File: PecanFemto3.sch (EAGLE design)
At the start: 35 parts, among them U1 TPS62203DBVT

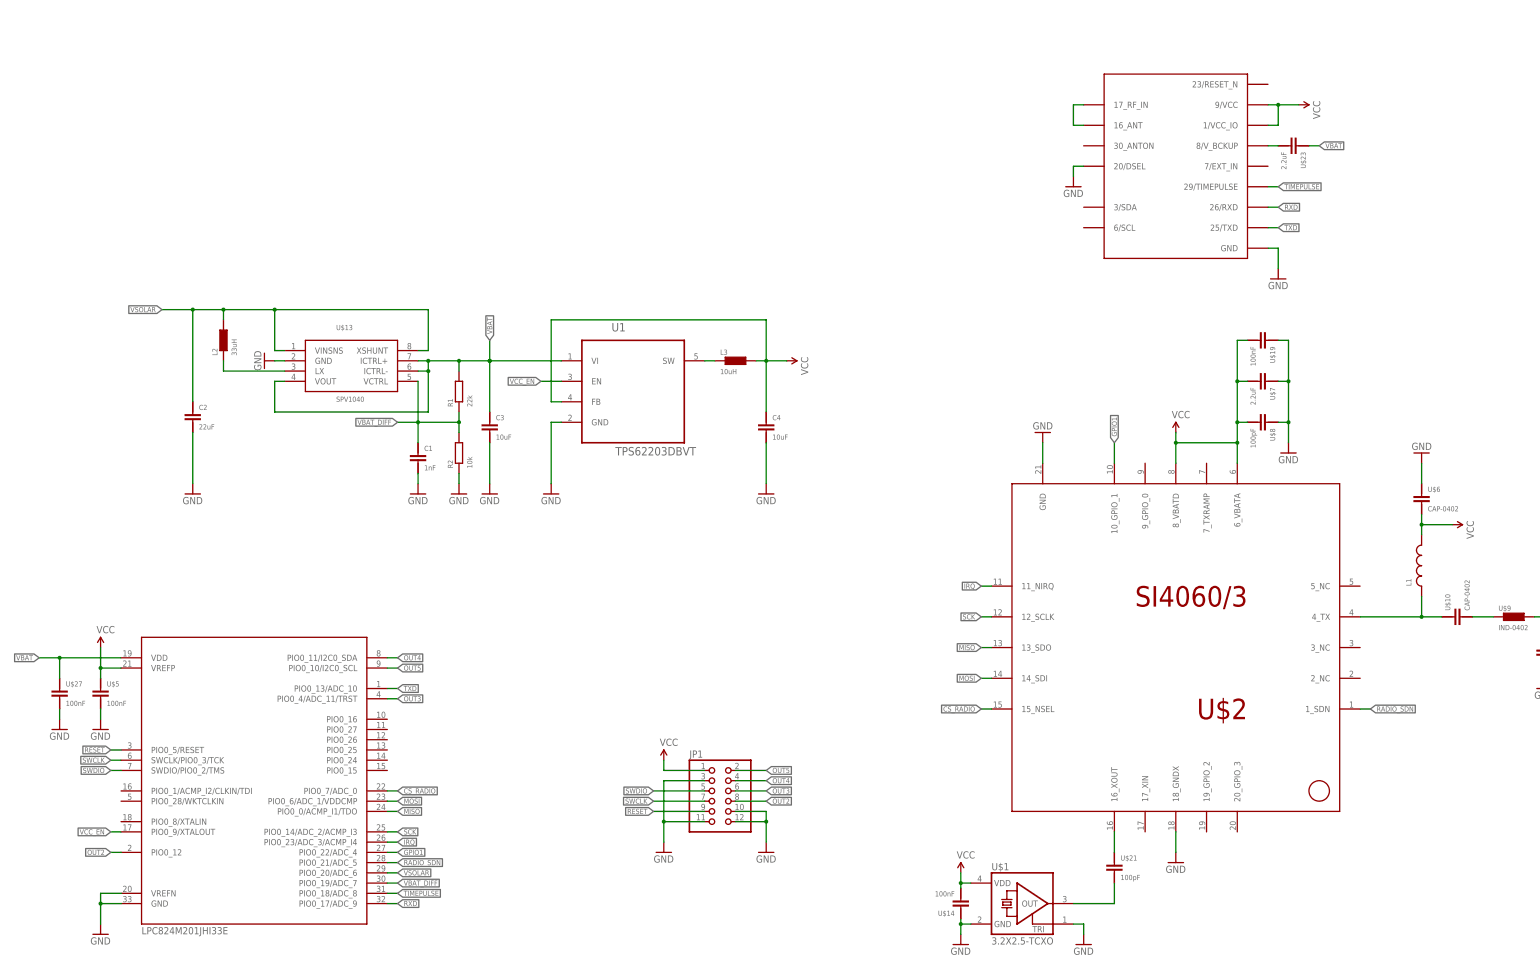
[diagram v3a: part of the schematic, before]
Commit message: Moved parts around, added MOSFET switch for GPS
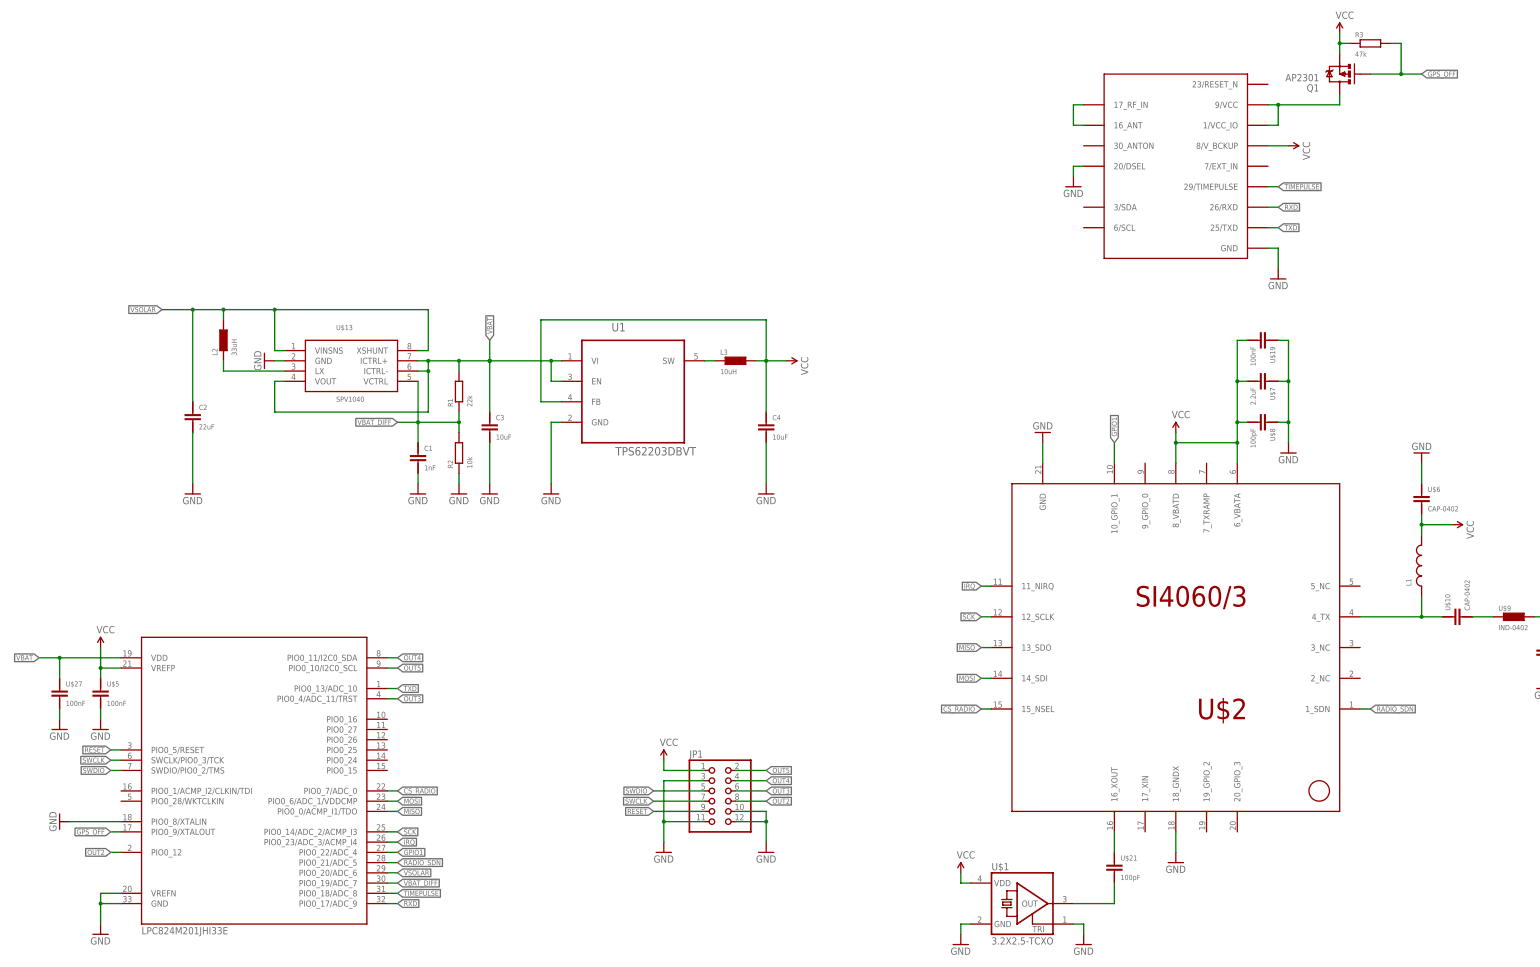
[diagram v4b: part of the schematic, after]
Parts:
- removed U$14: 100nF, sven:CAP-0402
- removed U$23: 2.2uF, sven:CAP-0603
- added Q1: AP2301, PecanPico6:MOSFET-PCHANNEL
- added R3: 47k, PecanPico6:RES-0402
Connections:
- removed net N$1: U$23.1, U$3.8/V_BCKUP
- removed net VCC_EN: U$4.PIO0_9/XTALOUT, U1.EN
- new net GPS_OFF: Q1.G, R3.2, U$4.PIO0_9/XTALOUT
- new net N$16: Q1.D, U$3.1/VCC_IO, U$3.9/VCC
- net GND: now also U$4.PIO0_8/XTALIN; no longer U$14.2
- net VBAT: now also U1.EN; no longer U$23.2
- net VCC: now also Q1.S, R3.1, U$3.8/V_BCKUP; no longer U$14.1, U$3.1/VCC_IO, U$3.9/VCC
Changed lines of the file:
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@@
 <part name="GND12" library="SparkFun-Aesthetics" deviceset="GND" device=""/>
 <part name="GND13" library="SparkFun-Aesthetics" deviceset="GND" device=""/>
-<part name="SUPPLY3" library="SparkFun-Aesthetics" deviceset="VCC" device=""/>
 <part name="SUPPLY4" library="SparkFun-Aesthetics" deviceset="VCC" device=""/>
 <part name="GND7" library="SparkFun-Aesthetics" deviceset="GND" device=""/>
@@
 <part name="U$27" library="sven" deviceset="CAP-0402" device="" value="100nF"/>
 <part name="GND24" library="SparkFun-Aesthetics" deviceset="GND" device=""/>
-<part name="U$23" library="sven" deviceset="CAP-0603" device="" value="2.2uF"/>
 <part name="U$7" library="sven" deviceset="CAP-0402" device="" value="2.2uF"/>
 <part name="SUPPLY7" library="SparkFun-Aesthetics" deviceset="VCC" device=""/>
-<part name="U$14" library="sven" deviceset="CAP-0402" device="" value="100nF"/>
+<part name="Q1" library="PecanPico6" deviceset="MOSFET-PCHANNEL" device="" value="AP2301"/>
+<part name="R3" library="PecanPico6" deviceset="RES-0402" device="" value="47k"/>
+<part name="SUPPLY3" library="SparkFun-Aesthetics" deviceset="VCC" device=""/>
+<part name="SUPPLY8" library="SparkFun-Aesthetics" deviceset="VCC" device=""/>
+<part name="GND25" library="SparkFun-Aesthetics" deviceset="GND" device=""/>
 </parts>
 <sheets>
@@
 <instance part="GND12" gate="1" x="193.04" y="154.94"/>
 <instance part="GND13" gate="1" x="243.84" y="132.08"/>
-<instance part="SUPPLY3" gate="G$1" x="248.92" y="175.26" rot="R270"/>
 <instance part="SUPPLY4" gate="G$1" x="218.44" y="93.98"/>
 <instance part="GND7" gate="1" x="246.38" y="88.9"/>
@@
 <instance part="U$27" gate="G$1" x="-58.42" y="30.48"/>
 <instance part="GND24" gate="1" x="-58.42" y="20.32"/>
-<instance part="U$23" gate="G$1" x="248.92" y="165.1" rot="R270"/>
 <instance part="U$7" gate="G$1" x="241.3" y="106.68" rot="R270"/>
 <instance part="SUPPLY7" gate="G$1" x="91.44" y="12.7"/>
-<instance part="U$14" gate="G$1" x="165.1" y="-24.13" rot="R180"/>
+<instance part="Q1" gate="G$1" x="259.08" y="182.88" rot="R180"/>
+<instance part="R3" gate="G$1" x="266.7" y="190.5"/>
+<instance part="SUPPLY3" gate="G$1" x="259.08" y="193.04"/>
+<instance part="SUPPLY8" gate="G$1" x="246.38" y="165.1" rot="R270"/>
+<instance part="GND25" gate="1" x="-58.42" y="-2.54" rot="R270"/>
 </instances>
 <busses>
@@
 <pinref part="U$1" gate="G$1" pin="GND"/>
 <wire x1="165.1" y1="-27.94" x2="167.64" y2="-27.94" width="0.1524" layer="91"/>
-<pinref part="U$14" gate="G$1" pin="2"/>
-<wire x1="165.1" y1="-27.94" x2="165.1" y2="-26.67" width="0.1524" layer="91"/>
-<junction x="165.1" y="-27.94"/>
 </segment>
 <segment>
@@
 <pinref part="GND24" gate="1" pin="GND"/>
 </segment>
+<segment>
+<pinref part="U$4" gate="G$1" pin="PIO0_8/XTALIN"/>
+<wire x1="-43.18" y1="-2.54" x2="-55.88" y2="-2.54" width="0.1524" layer="91"/>
+<pinref part="GND25" gate="1" pin="GND"/>
+</segment>
 </net>
 <net name="N$4" class="0">
@@
 <junction x="279.4" y="71.12"/>
 <pinref part="SUPPLY1" gate="G$1" pin="VCC"/>
-</segment>
-<segment>
-<pinref part="U$3" gate="G$1" pin="1/VCC_IO"/>
-<wire x1="241.3" y1="170.18" x2="243.84" y2="170.18" width="0.1524" layer="91"/>
-<wire x1="243.84" y1="170.18" x2="243.84" y2="175.26" width="0.1524" layer="91"/>
-<pinref part="U$3" gate="G$1" pin="9/VCC"/>
-<wire x1="243.84" y1="175.26" x2="241.3" y2="175.26" width="0.1524" layer="91"/>
-<junction x="243.84" y="175.26"/>
-<wire x1="243.84" y1="175.26" x2="248.92" y2="175.26" width="0.1524" layer="91"/>
-<pinref part="SUPPLY3" gate="G$1" pin="VCC"/>
 </segment>
 <segment>
@@
 <wire x1="165.1" y1="-17.78" x2="165.1" y2="-15.24" width="0.1524" layer="91"/>
 <wire x1="167.64" y1="-17.78" x2="165.1" y2="-17.78" width="0.1524" layer="91"/>
-<pinref part="U$14" gate="G$1" pin="1"/>
-<wire x1="165.1" y1="-17.78" x2="165.1" y2="-19.05" width="0.1524" layer="91"/>
-<junction x="165.1" y="-17.78"/>
 </segment>
 <segment>
 <pinref part="U1" gate="A" pin="FB"/>
-<wire x1="66.04" y1="101.6" x2="63.5" y2="101.6" width="0.1524" layer="91"/>
-<wire x1="63.5" y1="101.6" x2="63.5" y2="121.92" width="0.1524" layer="91"/>
-<wire x1="63.5" y1="121.92" x2="116.84" y2="121.92" width="0.1524" layer="91"/>
+<wire x1="66.04" y1="101.6" x2="60.96" y2="101.6" width="0.1524" layer="91"/>
+<wire x1="60.96" y1="101.6" x2="60.96" y2="121.92" width="0.1524" layer="91"/>
+<wire x1="60.96" y1="121.92" x2="116.84" y2="121.92" width="0.1524" layer="91"/>
 <pinref part="L3" gate="G$1" pin="2"/>
 <wire x1="114.3" y1="111.76" x2="116.84" y2="111.76" width="0.1524" layer="91"/>
@@
 <wire x1="91.44" y1="10.16" x2="91.44" y2="12.7" width="0.1524" layer="91"/>
 <pinref part="SUPPLY7" gate="G$1" pin="VCC"/>
+</segment>
+<segment>
+<pinref part="Q1" gate="G$1" pin="S"/>
+<wire x1="259.08" y1="187.96" x2="259.08" y2="190.5" width="0.1524" layer="91"/>
+<pinref part="R3" gate="G$1" pin="1"/>
+<wire x1="259.08" y1="190.5" x2="259.08" y2="193.04" width="0.1524" layer="91"/>
+<wire x1="259.08" y1="190.5" x2="261.62" y2="190.5" width="0.1524" layer="91"/>
+<junction x="259.08" y="190.5"/>
+<pinref part="SUPPLY3" gate="G$1" pin="VCC"/>
+</segment>
+<segment>
+<pinref part="U$3" gate="G$1" pin="8/V_BCKUP"/>
+<pinref part="SUPPLY8" gate="G$1" pin="VCC"/>
+<wire x1="246.38" y1="165.1" x2="241.3" y2="165.1" width="0.1524" layer="91"/>
 </segment>
 </net>
@@
 <pinref part="C3" gate="G$1" pin="2"/>
 <pinref part="U1" gate="A" pin="VI"/>
-<wire x1="48.26" y1="111.76" x2="66.04" y2="111.76" width="0.1524" layer="91"/>
+<wire x1="48.26" y1="111.76" x2="63.5" y2="111.76" width="0.1524" layer="91"/>
 <junction x="48.26" y="111.76"/>
+<pinref part="U1" gate="A" pin="EN"/>
+<wire x1="63.5" y1="111.76" x2="66.04" y2="111.76" width="0.1524" layer="91"/>
+<wire x1="66.04" y1="106.68" x2="63.5" y2="106.68" width="0.1524" layer="91"/>
+<wire x1="63.5" y1="106.68" x2="63.5" y2="111.76" width="0.1524" layer="91"/>
+<junction x="63.5" y="111.76"/>
 </segment>
 <segment>
@@
 <junction x="-58.42" y="38.1"/>
 <label x="-63.5" y="38.1" size="1.27" layer="95" rot="R180" xref="yes"/>
-</segment>
-<segment>
-<wire x1="251.46" y1="165.1" x2="254" y2="165.1" width="0.1524" layer="91"/>
-<label x="254" y="165.1" size="1.27" layer="95" xref="yes"/>
-<pinref part="U$23" gate="G$1" pin="2"/>
 </segment>
 </net>
@@
 </segment>
 </net>
-<net name="VCC_EN" class="0">
-<segment>
-<pinref part="U1" gate="A" pin="EN"/>
-<wire x1="66.04" y1="106.68" x2="60.96" y2="106.68" width="0.1524" layer="91"/>
-<label x="60.96" y="106.68" size="1.27" layer="95" rot="R180" xref="yes"/>
+<net name="N$15" class="0">
+<segment>
+<pinref part="U1" gate="A" pin="SW"/>
+<pinref part="L3" gate="G$1" pin="1"/>
+<wire x1="104.14" y1="111.76" x2="101.6" y2="111.76" width="0.1524" layer="91"/>
+</segment>
+</net>
+<net name="GPS_OFF" class="0">
+<segment>
+<pinref part="Q1" gate="G$1" pin="G"/>
+<wire x1="266.7" y1="182.88" x2="274.32" y2="182.88" width="0.1524" layer="91"/>
+<pinref part="R3" gate="G$1" pin="2"/>
+<wire x1="274.32" y1="182.88" x2="279.4" y2="182.88" width="0.1524" layer="91"/>
+<wire x1="271.78" y1="190.5" x2="274.32" y2="190.5" width="0.1524" layer="91"/>
+<wire x1="274.32" y1="190.5" x2="274.32" y2="182.88" width="0.1524" layer="91"/>
+<junction x="274.32" y="182.88"/>
+<label x="279.4" y="182.88" size="1.27" layer="95" xref="yes"/>
 </segment>
 <segment>
@@
 </segment>
 </net>
-<net name="N$15" class="0">
-<segment>
-<pinref part="U1" gate="A" pin="SW"/>
-<pinref part="L3" gate="G$1" pin="1"/>
-<wire x1="104.14" y1="111.76" x2="101.6" y2="111.76" width="0.1524" layer="91"/>
-</segment>
-</net>
-<net name="N$1" class="0">
-<segment>
-<pinref part="U$3" gate="G$1" pin="8/V_BCKUP"/>
-<wire x1="241.3" y1="165.1" x2="243.84" y2="165.1" width="0.1524" layer="91"/>
-<pinref part="U$23" gate="G$1" pin="1"/>
-</segment>
-</net>
+<net name="N$16" class="0">
+<segment>
+<pinref part="U$3" gate="G$1" pin="1/VCC_IO"/>
+<wire x1="241.3" y1="170.18" x2="243.84" y2="170.18" width="0.1524" layer="91"/>
+<pinref part="U$3" gate="G$1" pin="9/VCC"/>
+<pinref part="Q1" gate="G$1" pin="D"/>
+<wire x1="259.08" y1="177.8" x2="259.08" y2="175.26" width="0.1524" layer="91"/>
+<wire x1="259.08" y1="175.26" x2="243.84" y2="175.26" width="0.1524" layer="91"/>
+<wire x1="243.84" y1="175.26" x2="241.3" y2="175.26" width="0.1524" layer="91"/>
+<wire x1="243.84" y1="170.18" x2="243.84" y2="175.26" width="0.1524" layer="91"/>
+<junction x="243.84" y="175.26"/>
+</segment>
+</net>

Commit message: Moved all parts around
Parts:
- added U$14: EVA7M, eva7m:EVA7M
- added U$16: 100nF, sven:CAP-0402
- U$3: value UBLOX_CAM -> JTI_ANTENNA-1575AT43A40; device Ava:UBLOX_CAM -> Ava:JTI_ANTENNA-1575AT43A40
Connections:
- removed net N$11: U$3.16_ANT, U$3.17_RF_IN
- removed net TIMEPULSE: U$3.29/TIMEPULSE, U$4.PIO0_18/ADC_8
- new net N$1: U$14.RF_IN, U$3.FEED
- net CS_RADIO: now also U$4.PIO0_14/ADC_2/ACMP_I3, U$4.PIO0_6/ADC_1/VDDCMP; no longer U$4.PIO0_7/ADC_0
- net GND: now also U$14.GND, U$14.RF_GND, U$16.2; no longer U$3.20/DSEL, U$3.GND
- net GPIO1: now also U$4.PIO0_13/ADC_10, U$4.PIO0_19/ADC_7; no longer U$4.PIO0_22/ADC_4
- net IRQ: now also U$4.PIO0_20/ADC_6; no longer U$4.PIO0_23/ADC_3/ACMP_I4
- net MISO: now also U$4.PIO0_22/ADC_4; no longer U$4.PIO0_0/ACMP_I1/TDO
- net MOSI: now also U$4.PIO0_0/ACMP_I1/TDO, U$4.PIO0_23/ADC_3/ACMP_I4; no longer U$4.PIO0_6/ADC_1/VDDCMP
- net N$16: now also U$14.VCC, U$14.VCC_IO, U$16.1; no longer U$3.1/VCC_IO, U$3.9/VCC
- net RADIO_SDN: no longer U$4.PIO0_21/ADC_5
- net RXD: now also U$14.RX_MOSI; no longer U$3.26/RXD, U$4.PIO0_17/ADC_9
- net SCK: now also U$4.PIO0_21/ADC_5; no longer U$4.PIO0_14/ADC_2/ACMP_I3
- net TXD: now also U$14.TX_MISO; no longer U$3.25/TXD, U$4.PIO0_13/ADC_10
- net VBAT_DIFF: now also U$4.PIO0_17/ADC_9; no longer U$4.PIO0_19/ADC_7
- net VCC: now also U$14.VCC_BCKP; no longer U$3.8/V_BCKUP
- net VSOLAR: now also U$4.PIO0_18/ADC_8; no longer U$4.PIO0_20/ADC_6
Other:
- moved on the sheet: Q1, R3

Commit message: Removed GPS-Switch-MOSFET and connected parts
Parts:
- removed PAD1, PAD2, PAD3: (no value), PecanFemto4:SMD2
- removed Q1: AP2301, PecanPico6:MOSFET-PCHANNEL
- removed R3: 47k, PecanPico6:RES-0402
- removed U$27, U$5: 100nF, sven:CAP-0402
- removed U$3: JTI_ANTENNA-1575AT43A40, Ava:JTI_ANTENNA-1575AT43A40
- added PAD4, PAD5: (no value), PecanFemto4:SMD2
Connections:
- removed net GPS_OFF: Q1.G, R3.2, U$4.PIO0_9/XTALOUT
- removed net N$16: Q1.D, U$14.VCC, U$14.VCC_IO, U$16.1
- new net VCC_GPS: U$14.VCC, U$14.VCC_IO, U$16.1, U$4.PIO0_12, U$4.PIO0_13/ADC_10
- net CS_RADIO: now also U$4.PIO0_10/I2C0_SCL; no longer U$4.PIO0_14/ADC_2/ACMP_I3, U$4.PIO0_6/ADC_1/VDDCMP
- net GND: now also PAD5.P; no longer PAD1.P, PAD3.P, U$27.1, U$5.1
- net GPIO1: now also U$4.PIO0_15; no longer U$4.PIO0_13/ADC_10, U$4.PIO0_19/ADC_7
- net IRQ: now also U$4.PIO0_25; no longer U$4.PIO0_20/ADC_6
- net MISO: now also U$4.PIO0_27; no longer U$4.PIO0_22/ADC_4
- net MOSI: now also U$4.PIO0_16; no longer U$4.PIO0_0/ACMP_I1/TDO, U$4.PIO0_23/ADC_3/ACMP_I4
- net N$1: now also PAD4.P; no longer U$3.FEED
- net N$3: no longer PAD2.P
- net OUT2: no longer U$4.PIO0_12
- net OUT3: no longer U$4.PIO0_4/ADC_11/TRST
- net OUT4: no longer U$4.PIO0_11/I2C0_SDA
- net OUT5: no longer U$4.PIO0_10/I2C0_SCL
- net RXD: now also U$4.PIO0_21/ADC_5
- net SCK: now also U$4.PIO0_26; no longer U$4.PIO0_21/ADC_5
- net TXD: now also U$4.PIO0_14/ADC_2/ACMP_I3
- net VBAT: no longer U$27.2, U$4.VDD
- net VBAT_DIFF: now also U$4.PIO0_4/ADC_11/TRST; no longer U$4.PIO0_17/ADC_9
- net VCC: now also U$4.VDD; no longer Q1.S, R3.1, U$5.2
- net VSOLAR: now also U$4.PIO0_17/ADC_9; no longer U$4.PIO0_18/ADC_8

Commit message: Routed parts
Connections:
- net RXD: now also U$4.PIO0_0/ACMP_I1/TDO; no longer U$4.PIO0_21/ADC_5
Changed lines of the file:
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@@
 </segment>
 <segment>
-<label x="25.4" y="-12.7" size="1.27" layer="95" xref="yes"/>
-<pinref part="U$4" gate="G$1" pin="PIO0_21/ADC_5"/>
-<wire x1="25.4" y1="-12.7" x2="22.86" y2="-12.7" width="0.1524" layer="91"/>
+<label x="25.4" y="0" size="1.27" layer="95" xref="yes"/>
+<pinref part="U$4" gate="G$1" pin="PIO0_0/ACMP_I1/TDO"/>
+<wire x1="25.4" y1="0" x2="22.86" y2="0" width="0.1524" layer="91"/>
 </segment>
 </net>
@@
 </segment>
 <segment>
+<label x="25.4" y="-5.08" size="1.27" layer="95" xref="yes"/>
 <pinref part="U$4" gate="G$1" pin="PIO0_14/ADC_2/ACMP_I3"/>
 <wire x1="22.86" y1="-5.08" x2="25.4" y2="-5.08" width="0.1524" layer="91"/>
-<label x="25.4" y="-5.08" size="1.27" layer="95" xref="yes"/>
 </segment>
 </net>

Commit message: Updated libraries, moved parts around, routed
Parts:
- added ANTENNA, GND, GND15, VBAT: (no value), PecanFemto4:SMD2
- added IC4: SI4060/3, PecanFemto4:SI4060/3
- added TCXO: TXC 7Z-26.000MCG-T, tcxo:TXC_7Z
- IC1: value SPV1040 -> SPV1040T
- L2: value 33uH -> LPS3015-103MRB
- L3: value 10uH -> LPS3015-103MRB
- U$1: value 3.2X2.5-TCXO -> 100nF; device Ava:3.2X2.5-TCXO -> sven:CAP-0402
- U$2: value SI4060/3 -> 100pF; device PecanFemto4:SI4060/3 -> sven:CAP-0402
- renumbered U$13 to IC1, U$14 to IC3, U$4 to IC5
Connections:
- removed net OUT5: JP1.2
- new net N$7: IC4.17_XIN, U$2.2
- new net OUT1: IC5.PIO0_28/WKTCLKIN, JP1.8
- net CS_RADIO: now also IC4.15_NSEL; no longer U$2.15_NSEL
- net GND: now also GND.P, GND15.P, IC3.GND_PAD1, IC3.GND_PAD2, IC3.GND_PAD3, IC3.GND_PAD4, IC3.GND_PAD5, IC3.GND_PAD6, IC3.GND_PAD7, IC4.18_GNDX, IC4.GND, TCXO.AFC, TCXO.GND, U$1.1; no longer U$1.GND, U$1.TRI, U$2.18_GNDX, U$2.GND
- net GPIO1: now also IC4.10_GPIO_1, IC5.PIO0_1/ACMP_I2/CLKIN/TDI; no longer IC5.PIO0_15, U$2.10_GPIO_1
- net IRQ: now also IC4.11_NIRQ; no longer U$2.11_NIRQ
- net MISO: now also IC4.13_SDO; no longer U$2.13_SDO
- net MOSI: now also IC4.14_SDI; no longer U$2.14_SDI
- net N$10: now also IC4.16_XOUT; no longer U$2.16_XOUT
- net N$2: now also IC4.4_TX; no longer U$2.4_TX
- net N$3: now also ANTENNA.P
- net N$9: now also TCXO.OUT, U$2.1; no longer U$1.OUT
- net OUT2: now also IC5.PIO0_11/I2C0_SDA, JP1.6; no longer JP1.8
- net OUT3: now also JP1.4; no longer JP1.6
- net OUT4: now also JP1.2; no longer JP1.4
- net RADIO_SDN: now also IC4.1_SDN; no longer U$2.1_SDN
- net RXD: now also IC5.PIO0_14/ADC_2/ACMP_I3; no longer IC5.PIO0_0/ACMP_I1/TDO
- net SCK: now also IC4.12_SCLK; no longer U$2.12_SCLK
- net TXD: now also IC5.PIO0_0/ACMP_I1/TDO; no longer IC5.PIO0_14/ADC_2/ACMP_I3
- net VBAT: now also VBAT.P
- net VCC: now also IC4.6_VBATA, IC4.8_VBATD, TCXO.VCC, U$1.2; no longer U$1.VDD, U$2.6_VBATA, U$2.8_VBATD
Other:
- note added: "Operating Vcc 3.3V TPS62203DBV 2.5V TPS62205DBV 1.8V TPS62202DBV"
- moved on the sheet: C4, L3, U1
